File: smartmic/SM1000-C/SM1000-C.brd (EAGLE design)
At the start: 65 x 90 mm, 178 parts, among them CN1 HDR100-3, CN10 MJ-3523-SMT, CN11 HDR100-3, CN12 DF11-16DS, CN2 MOLEX-MINI-B-SMT, CN3 RASM712PX, CN4 RJ-45, CN5 MJ-3523-SMT, CN6 MJ-3523-SMT, CN7 MJ-3523-SMT, CN8 MJ-3523-SMT, CN9 MJ-3523-SMT, J1 JMP-2PIN, J3 JMP-2PIN, J4 JMP-2PIN, J5 JMP-2PIN, P1 TPAD50, P10 TPAD50, P11 TPAD50, P12 TPAD50, P13 TPAD50, P14 TPAD50, P15 TPAD50, P16 TPAD50, P17 TPAD50, P18 TPAD50, P19 TPAD50, P2 TPAD50, P20 TPAD50, P3 TPAD50, P4 TPAD50, P5 TPAD50, P6 TPAD50, P7 TPAD50, P8 TPAD50, P9 TPAD50, SW1 SW-BOURNS-7914S, SW2 SW-BOURNS-7914S, SW3 DPDT, SW4 SW-BOURNS-7914S, T1 SM-LP-5001, T2 SM-LP-5001, U1 STM32F405, U2 LD3985M33R, U3 STMPS2141, U4 EMIF02-USB03F2, U5 TPS54329E, U6 LMV341, U7 LMV341, U8 LM386M-1, U9 LMV341

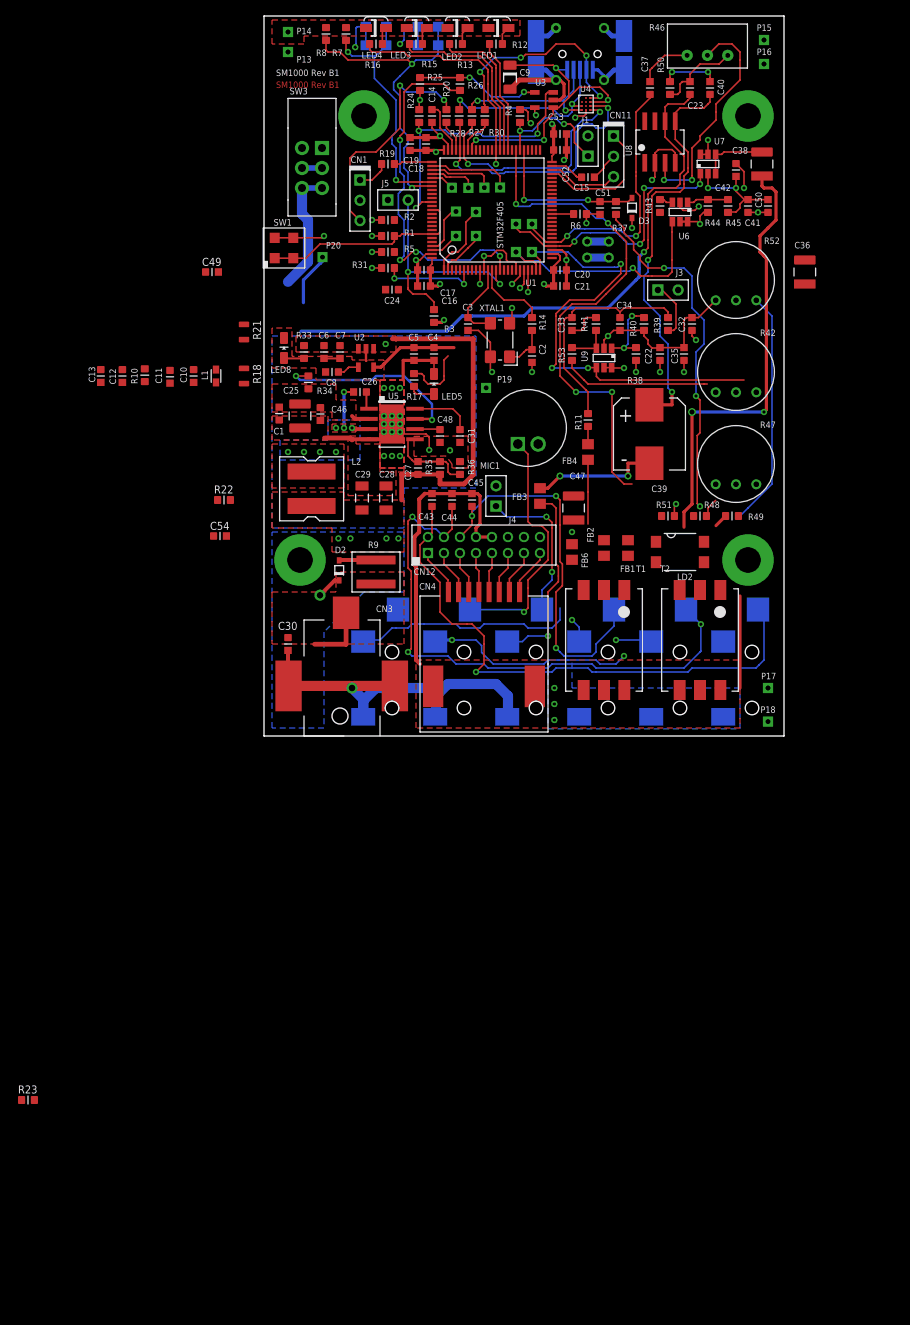
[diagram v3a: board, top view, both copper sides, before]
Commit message: Update Change-Log-C.txt #53 & #55  RGB 09/11/2014
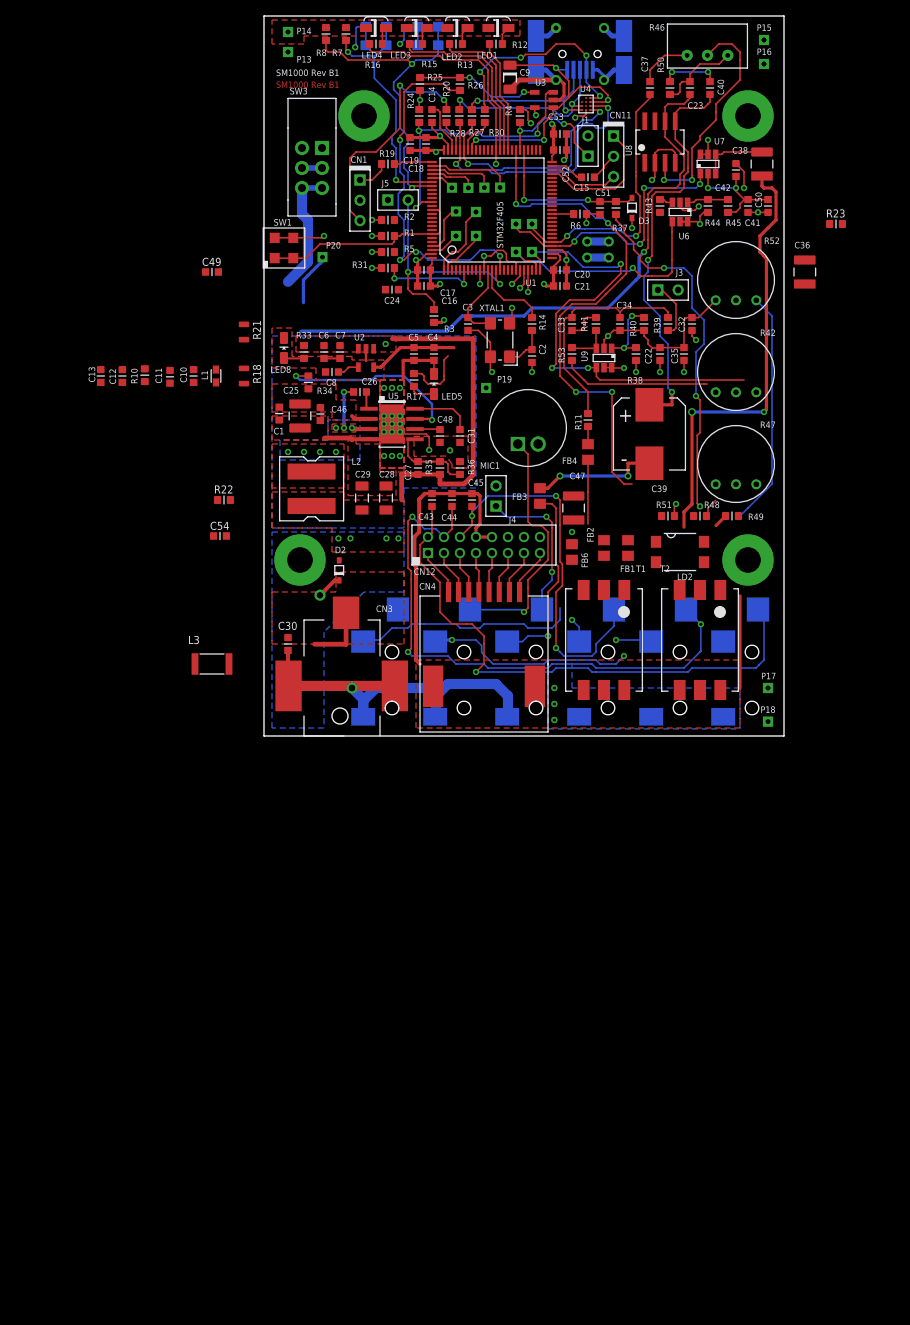
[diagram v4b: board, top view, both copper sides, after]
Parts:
- removed R9: 10,5%,1218, SM1000:RCL1218
- added L3: 100uH, _RoweTel:CBC3225T101MR
- moved R23 149.0 mm to (71.5, 64.0)
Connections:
- net +VEXT renamed N$15
- net N$24: now also L3.2; no longer R9.2
- net N$77: now also L3.1; no longer R9.1
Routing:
- net N$24: track 4.62 -> 0.07 mm
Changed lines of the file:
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@@
 <attribute name="VALUE" x="0.9625" y="12.75" size="1" layer="27" font="vector" ratio="10" rot="R270"/>
-</element>
-<element name="R9" library="SM1000" package="RCL1218" value="10,5%,1218" x="14" y="20.5" smashed="yes" rot="R90">
-<attribute name="NAME" x="13" y="23.5" size="0.8128" layer="25" ratio="10"/>
-<attribute name="VALUE" x="19" y="17.5" size="1" layer="27" ratio="10" rot="R90"/>
 </element>
 <element name="R11" library="AA-ipc-7351-resistor" package="RESC1608X55N" value="100,1%" x="40.5" y="39.5" smashed="yes" rot="R90">
@@
 <element name="R22" library="AA-ipc-7351-resistor" package="RESC1608X55N" value="22.1K,1%" x="-5" y="29.5"/>
 <element name="C54" library="AA-ipc-7351-capacitor" package="CAPC1608X92N" value="1nF,16V" x="-5.5" y="25"/>
-<element name="R23" library="AA-ipc-7351-resistor" package="RESC1608X55N" value="10K,1%" x="-29.5" y="-45.5"/>
+<element name="R23" library="AA-ipc-7351-resistor" package="RESC1608X55N" value="10K,1%" x="71.5" y="64"/>
+<element name="L3" library="_RoweTel" package="CBC3225T101MR" value="100uH" x="-6.5" y="9"/>
 </elements>
 <signals>
@@
 <wire x1="35.7" y1="58.1" x2="39.7" y2="58.1" width="0.2" layer="16"/>
 <contactref element="R23" pad="1"/>
-<wire x1="-30.3" y1="-45.5" x2="34" y2="58.25" width="0" layer="19" extent="1-1"/>
+<wire x1="70.7" y1="64" x2="34" y2="58.25" width="0" layer="19" extent="1-1"/>
 </signal>
 <signal name="+3.3V">
@@
 <wire x1="10.26" y1="11.47" x2="10.26" y2="15.4" width="0.6" layer="1"/>
 <contactref element="C30" pad="1"/>
-<contactref element="R9" pad="1"/>
 <polygon width="0.2" layer="1" isolate="0.3">
 <vertex x="1" y="18"/>
@@
 <vertex x="9" y="18"/>
 </polygon>
+<contactref element="L3" pad="1"/>
+<wire x1="3" y1="12.3" x2="-8.625" y2="9" width="0" layer="19" extent="1-1"/>
+<wire x1="6.33" y1="11.47" x2="3" y2="12.3" width="0" layer="19" extent="1-1"/>
 </signal>
 <signal name="N$4">
@@
 <signal name="N$24">
 <contactref element="D2" pad="A"/>
-<contactref element="R9" pad="2"/>
-<wire x1="14" y1="22" x2="9.45" y2="22" width="0.5" layer="1"/>
 <wire x1="9.45" y1="22" x2="9.4" y2="21.95" width="0.5" layer="1"/>
+<contactref element="L3" pad="2"/>
+<wire x1="9.4" y1="21.95" x2="-4.375" y2="9" width="0" layer="19" extent="1-1"/>
 </signal>
 <signal name="N$78">
@@
 <wire x1="37" y1="16" x2="54.15" y2="29.05" width="0" layer="19" extent="1-16"/>
 </signal>
-<signal name="+VEXT">
-<contactref element="SW3" pad="2"/>
-<contactref element="SW3" pad="5"/>
-<contactref element="D2" pad="C"/>
-<wire x1="7.25" y1="71" x2="4.75" y2="71" width="0.7" layer="16"/>
-<via x="7" y="17.6" extent="1-16" drill="0.8" diameter="1.42"/>
-<wire x1="7.25" y1="71" x2="9.5" y2="71" width="1.27" layer="15"/>
-<wire x1="9.5" y1="71" x2="9.5" y2="45.5" width="1.27" layer="15"/>
-<wire x1="9.5" y1="45.5" x2="7.5" y2="45.5" width="1.27" layer="15"/>
-<wire x1="7.5" y1="45.5" x2="7.5" y2="40.5" width="1.27" layer="15"/>
-<wire x1="7.5" y1="40.5" x2="13" y2="40.5" width="1.27" layer="15"/>
-<wire x1="13" y1="40.5" x2="13" y2="26.5" width="1.27" layer="15"/>
-<wire x1="13" y1="26.5" x2="13" y2="25.5" width="1.27" layer="15"/>
-<wire x1="13" y1="25.5" x2="13" y2="17.6" width="1.27" layer="15"/>
-<wire x1="13" y1="17.6" x2="7" y2="17.6" width="1.27" layer="15"/>
-<wire x1="9.4" y1="19.45" x2="8.85" y2="19.45" width="0.5" layer="1"/>
-<wire x1="8.85" y1="19.45" x2="7" y2="17.6" width="0.5" layer="1"/>
-</signal>
 <signal name="N$70">
 <contactref element="SW3" pad="3"/>
@@
 <wire x1="49.95" y1="67.05" x2="49.5" y2="67.05" width="0.2" layer="1"/>
 <contactref element="R23" pad="2"/>
-<wire x1="-28.7" y1="-45.5" x2="49.5" y2="67.05" width="0" layer="19" extent="1-1"/>
+<wire x1="72.3" y1="64" x2="49.5" y2="67.05" width="0" layer="19" extent="1-1"/>
+</signal>
+<signal name="N$15">
+<contactref element="SW3" pad="2"/>
+<contactref element="SW3" pad="5"/>
+<contactref element="D2" pad="C"/>
+<wire x1="7.25" y1="71" x2="4.75" y2="71" width="0.7" layer="16"/>
+<via x="7" y="17.6" extent="1-16" drill="0.8" diameter="1.42"/>
+<wire x1="7.25" y1="71" x2="9.5" y2="71" width="1.27" layer="15"/>
+<wire x1="9.5" y1="71" x2="9.5" y2="45.5" width="1.27" layer="15"/>
+<wire x1="9.5" y1="45.5" x2="7.5" y2="45.5" width="1.27" layer="15"/>
+<wire x1="7.5" y1="45.5" x2="7.5" y2="40.5" width="1.27" layer="15"/>
+<wire x1="7.5" y1="40.5" x2="13" y2="40.5" width="1.27" layer="15"/>
+<wire x1="13" y1="40.5" x2="13" y2="26.5" width="1.27" layer="15"/>
+<wire x1="13" y1="26.5" x2="13" y2="25.5" width="1.27" layer="15"/>
+<wire x1="13" y1="25.5" x2="13" y2="17.6" width="1.27" layer="15"/>
+<wire x1="13" y1="17.6" x2="7" y2="17.6" width="1.27" layer="15"/>
+<wire x1="9.4" y1="19.45" x2="8.85" y2="19.45" width="0.5" layer="1"/>
+<wire x1="8.85" y1="19.45" x2="7" y2="17.6" width="0.5" layer="1"/>
 </signal>
 </signals>

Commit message: Changes to PCB & Schematic. Added ststus line to each Change-Log-C item to reflect current status. RGB 09/15/14
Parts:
- CN3: value RASM712PX -> RASM722PX; device _RoweTel:RASM712PX -> _RoweTel:RASM722PX
- CN6, CN8: value MJ-3523-SMT -> SJ-3524-SMT; device _RoweTel:MJ-3523-SMT -> _RoweTel:SJ-3523-SMT
- moved CN6 110.4 mm to (-20.5, -66.5), flipped to the top, turned to 0 degrees
- moved CN8 81.1 mm to (-20.5, -52.0), flipped to the top, turned to 0 degrees
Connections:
- net N$62: now also CN8.4; no longer CN8.10
- net N$75: now also CN8.3
- net SPKR: now also CN6.4; no longer CN6.10
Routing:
- net N$62: track 19.3 -> 16.8 mm
- net N$75: track 24.3 -> 22.4 mm
- net SPKR: track 70.2 -> 69.1 mm

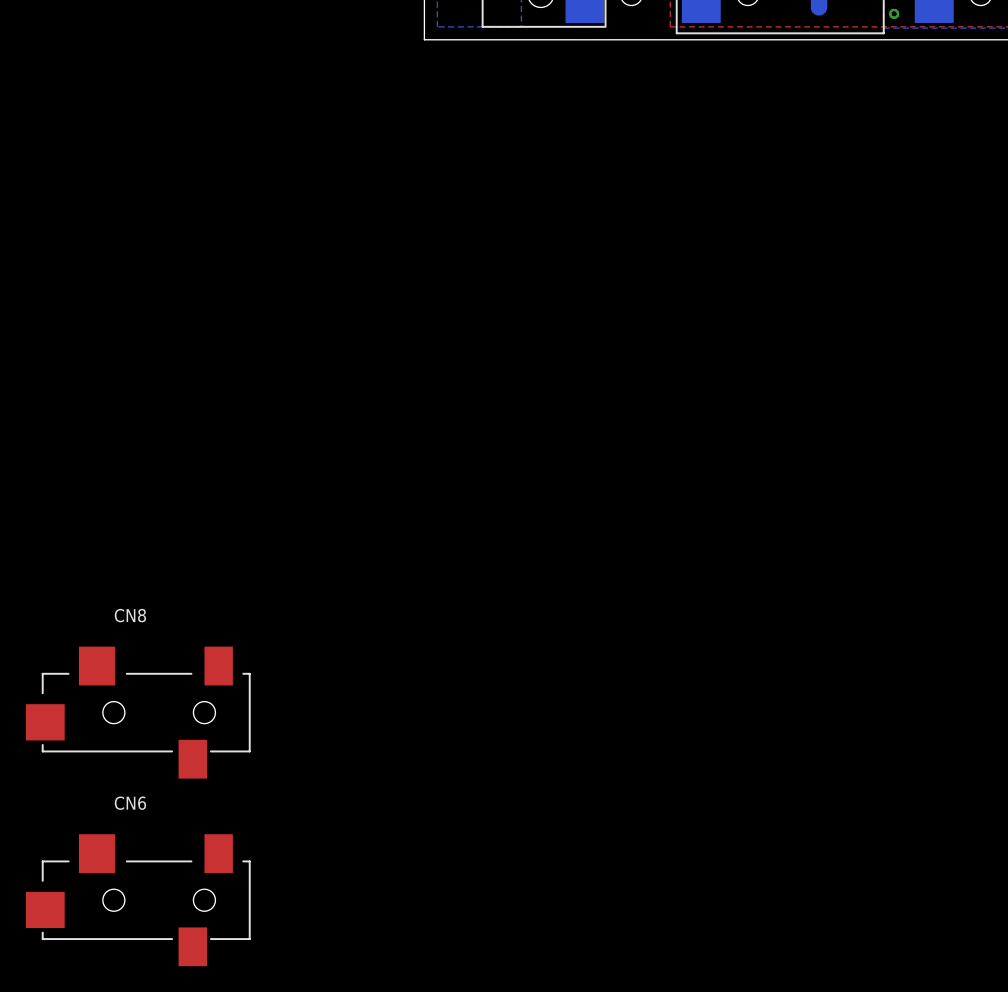
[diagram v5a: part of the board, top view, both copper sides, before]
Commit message: Update schematic to current time stamp RGB 09/15/14
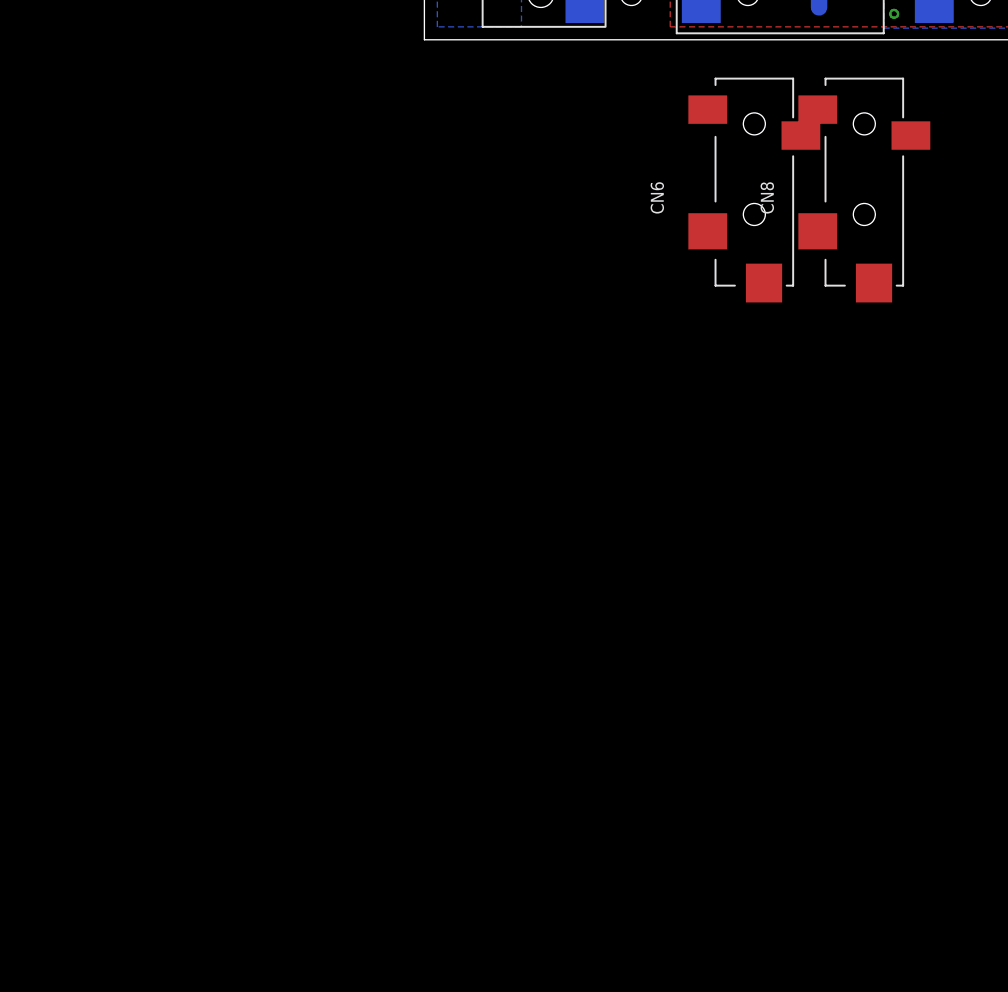
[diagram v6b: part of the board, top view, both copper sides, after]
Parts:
- moved CN6 72.9 mm to (25.5, -10.0), turned to 90 degrees
- moved CN8 68.8 mm to (34.0, -10.0), turned to 90 degrees
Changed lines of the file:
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@@
 <element name="R23" library="AA-ipc-7351-resistor" package="RESC1608X55N" value="10K,1%" x="71.5" y="64"/>
 <element name="L3" library="_RoweTel" package="CBC3225T101MR" value="100uH" x="-6.5" y="9"/>
-<element name="CN8" library="_RoweTel" package="SJ-3523-SMT" value="SJ-3524-SMT" x="-20.5" y="-52"/>
-<element name="CN6" library="_RoweTel" package="SJ-3523-SMT" value="SJ-3524-SMT" x="-20.5" y="-66.5"/>
+<element name="CN8" library="_RoweTel" package="SJ-3523-SMT" value="SJ-3524-SMT" x="34" y="-10" rot="R90"/>
+<element name="CN6" library="_RoweTel" package="SJ-3523-SMT" value="SJ-3524-SMT" x="25.5" y="-10" rot="R90"/>
 </elements>
 <signals>
@@
 <wire x1="2.31" y1="7.26" x2="3" y2="6.33" width="0" layer="19" extent="1-1"/>
 <wire x1="15.6" y1="7.26" x2="16.36" y2="6.26" width="0" layer="19" extent="1-1"/>
-<wire x1="-15.9" y1="-48.4" x2="3.07" y2="6.26" width="0" layer="19" extent="1-1"/>
+<wire x1="30.4" y1="-5.4" x2="3.07" y2="6.26" width="0" layer="19" extent="1-1"/>
 </signal>
 <signal name="NRST">
@@
 <wire x1="26.5" y1="8" x2="33.5" y2="8" width="0.2" layer="16"/>
 <contactref element="CN6" pad="4"/>
-<wire x1="26.5" y1="8" x2="-29.3" y2="-67.25" width="0" layer="19" extent="1-1"/>
+<wire x1="26.5" y1="8" x2="26.25" y2="-18.8" width="0" layer="19" extent="1-1"/>
 </signal>
 <signal name="N$49">
@@
 <wire x1="21.15" y1="6.21" x2="33.85" y2="6.21" width="0" layer="19" extent="1-1"/>
 <wire x1="19.5" y1="9" x2="21.15" y2="6.21" width="0" layer="19" extent="1-1"/>
-<wire x1="-15.9" y1="-62.9" x2="21.15" y2="6.21" width="0" layer="19" extent="1-1"/>
+<wire x1="21.9" y1="-5.4" x2="21.15" y2="6.21" width="0" layer="19" extent="1-1"/>
 </signal>
 <signal name="N$59">
@@
 <contactref element="FB1" pad="2"/>
 <contactref element="CN6" pad="2"/>
-<wire x1="45.5" y1="24.475" x2="-25.3" y2="-62.9" width="0" layer="19" extent="1-1"/>
+<wire x1="45.5" y1="24.475" x2="21.9" y2="-14.8" width="0" layer="19" extent="1-1"/>
 </signal>
 <signal name="N$72">
@@
 <contactref element="CN8" pad="3"/>
 <contactref element="CN8" pad="2"/>
-<wire x1="-25.3" y1="-48.4" x2="-17.9" y2="-55.6" width="0" layer="19" extent="1-1"/>
-<wire x1="32.3" y1="11.8" x2="-25.3" y2="-48.4" width="0" layer="19" extent="1-16"/>
+<wire x1="30.4" y1="-14.8" x2="37.6" y2="-7.4" width="0" layer="19" extent="1-1"/>
+<wire x1="32.3" y1="11.8" x2="30.4" y2="-14.8" width="0" layer="19" extent="1-16"/>
 </signal>
 <signal name="N$76">
@@
 <wire x1="36" y1="19.5" x2="36" y2="20.5" width="0.2" layer="16"/>
 <contactref element="CN8" pad="4"/>
-<wire x1="34.75" y1="18.25" x2="-29.3" y2="-52.75" width="0" layer="19" extent="1-16"/>
+<wire x1="34.75" y1="18.25" x2="34.75" y2="-18.8" width="0" layer="19" extent="1-16"/>
 </signal>
 <signal name="N$41">

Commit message: Update Eagle Files  RGB 9/24/14
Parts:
- added P21, P22, P23, P24: PAD070-035, _Coherix:PAD070-035
- CN6, CN8: device _RoweTel:SJ-3523-SMT -> _RoweTel:SJ-3524-SMT
- moved CN6 24.4 mm to (43.0, 7.00), flipped to the bottom, turned to 270 degrees
- moved CN8 19.2 mm to (25.0, 7.00), flipped to the bottom, turned to 270 degrees
- moved CN5 9.00 mm to (34.0, 8.00)
- moved CN7 9.00 mm to (61.0, 8.00)
- moved CN9 9.00 mm to (52.0, 8.00)
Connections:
- new net AVDD: C22.1, C32.1, C35.1, C41.1, C42.1, C50.1, J3.2, P24.1, R38.2, R44.2, U6.5, U6.6, U7.5, U7.6, U9.5
- new net AVSS: C10.2, C11.2, C12.2, C13.2, C22.2, C23.2, C32.2, C34.2, C35.2, C41.2, C42.2, C50.2, CN5.1, CN8.1, J4.2, MIC1.2, P23.1, R22.1, R40.2, R45.2, R46.1, R50.2, R52.1, T1.3, T2.3, U1.20, U6.2, U7.2, U8.2, U8.4, U9.2
- net GND: now also P22.1; no longer C10.2, C11.2, C12.2, C13.2, C22.2, C23.2, C32.2, C34.2, C35.2, C41.2, C42.2, C50.2, CN5.1, CN8.1, J4.2, MIC1.2, R22.1, R40.2, R45.2, R46.1, R50.2, R52.1, T1.3, T2.3, U1.20, U6.2, U7.2, U8.2, U8.4, U9.2
- net VDD: now also P21.1; no longer C22.1, C32.1, C35.1, C41.1, C42.1, C50.1, J3.2, R38.2, R44.2, U6.5, U6.6, U7.5, U7.6, U9.5
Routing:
- net GND: track 219.1 -> 127.1 mm, vias 41 -> 34
- net MIC: track 71.4 -> 26.7 mm, vias 3 -> 1
- net SPKR: track 69.1 -> 26.6 mm, vias 1 -> 0
- net AVSS: track 0.00 -> 41.9 mm, vias 0 -> 6
- net N$85: track 72.7 -> 44.6 mm
- net N$76: track 34.3 -> 8.02 mm, vias 2 -> 0
- net VDD: track 146.2 -> 126.0 mm, vias 27 -> 19
- net APTT: track 47.8 -> 35.9 mm, vias 3 -> 2
- net AVDD: track 0.00 -> 10.5 mm, vias 0 -> 5
- net N$60: track 31.4 -> 24.5 mm, vias 1 -> 0
- net N$72: track 4.48 -> 0.00 mm, vias 1 -> 0
- net N$75: track 22.4 -> 18.9 mm, vias 1 -> 0
- net N$73: track 3.07 -> 0.00 mm, vias 1 -> 0
